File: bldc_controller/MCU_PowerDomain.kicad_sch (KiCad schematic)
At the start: 10 parts, among them U2 STM32G474CEUx

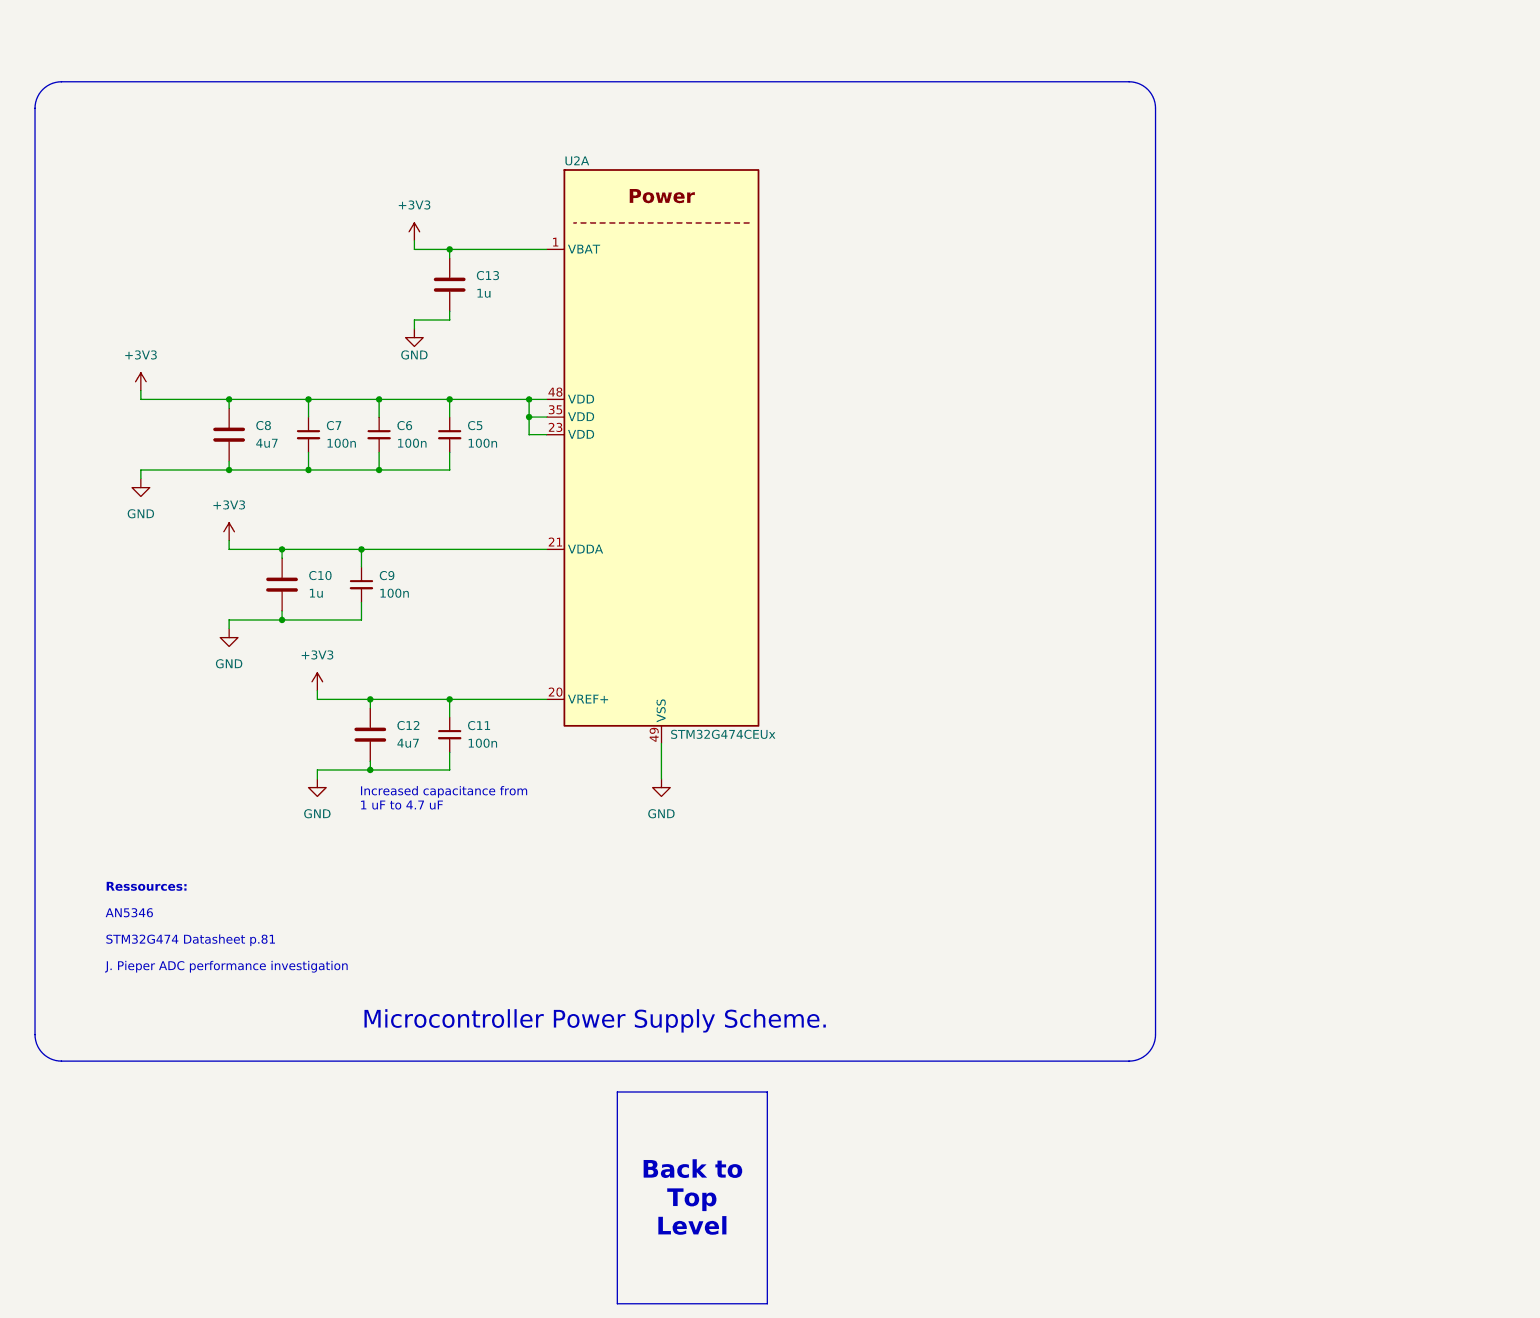
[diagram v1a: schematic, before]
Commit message: added temporary footprints and deleted extra files
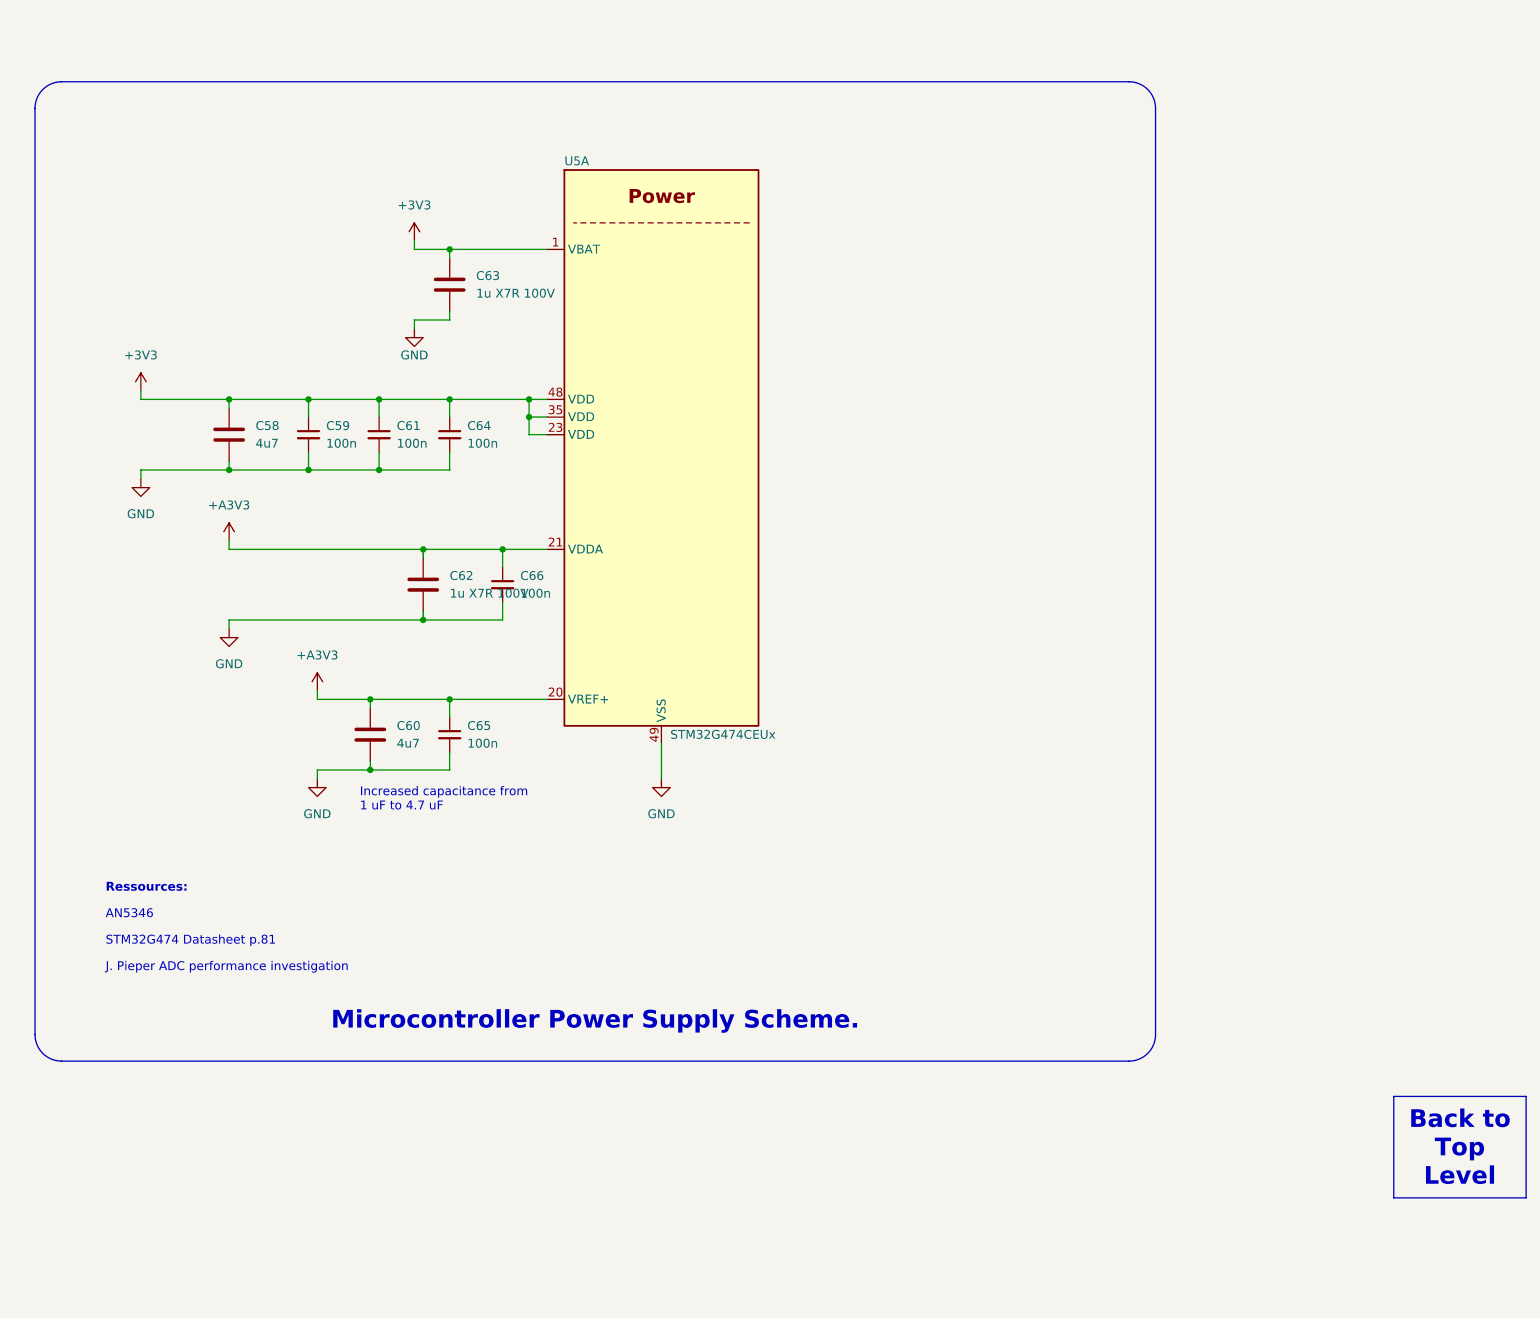
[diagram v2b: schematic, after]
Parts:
- C58: renamed from C8; footprint (none) -> Capacitor_SMD:C_0603_1608Metric
- C59: renamed from C7; footprint (none) -> Capacitor_SMD:C_0402_1005Metric
- C60: renamed from C12; footprint (none) -> Capacitor_SMD:C_0603_1608Metric
- C61: renamed from C6; footprint (none) -> Capacitor_SMD:C_0402_1005Metric
- C62: renamed from C10; value 1u -> 1u X7R 100V; footprint (none) -> Capacitor_SMD:C_0402_1005Metric
- C63: renamed from C13; value 1u -> 1u X7R 100V; footprint (none) -> Capacitor_SMD:C_0402_1005Metric
- C64: renamed from C5; footprint (none) -> Capacitor_SMD:C_0402_1005Metric
- C65: renamed from C11; footprint (none) -> Capacitor_SMD:C_0402_1005Metric
- C66: renamed from C9; footprint (none) -> Capacitor_SMD:C_0402_1005Metric
- renumbered U2 to U5
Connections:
- net +3V3: no longer C60.1, C62.1, C65.1, C66.1, U5.20 (VREF+), U5.21 (VDDA)
- new net +A3V3: C60.1, C62.1, C65.1, C66.1, U5.20 (VREF+), U5.21 (VDDA)
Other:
- moved on the sheet: C62, C66

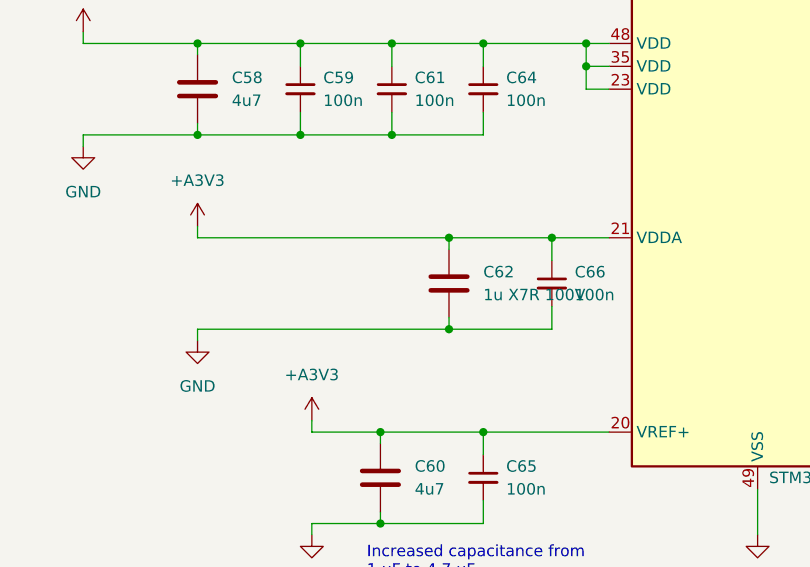
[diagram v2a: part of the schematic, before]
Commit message: added IPC-7351 compliant footprints and started routing
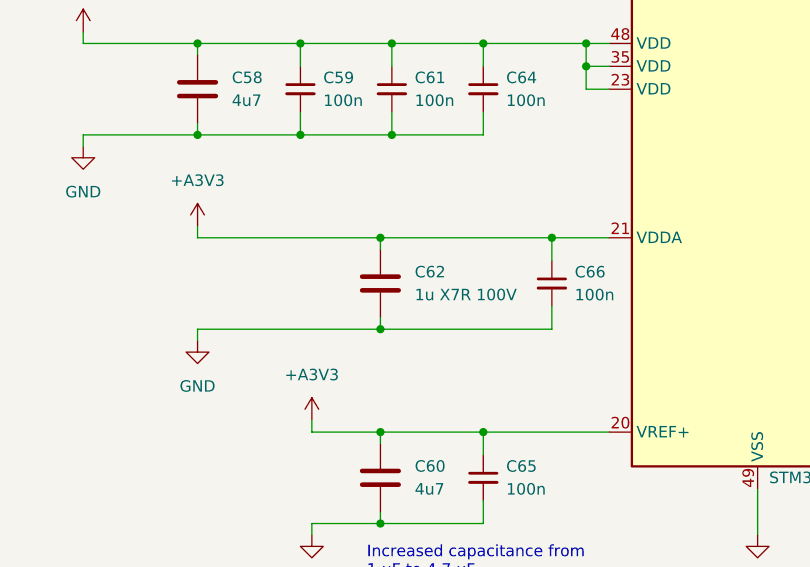
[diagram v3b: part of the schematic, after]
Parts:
- C58, C60: footprint Capacitor_SMD:C_0603_1608Metric -> 0_capacitor_smd:C_0603_1608_DensityHigh
- C59, C61, C62, C63, C64, C65, C66: footprint Capacitor_SMD:C_0402_1005Metric -> 0_capacitor_smd:C_0402_1005_DensityHigh
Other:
- moved on the sheet: C62
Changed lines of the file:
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@@
   (junction (at 109.22 66.04) (diameter 0) (color 0 0 0 0)
   )
-  (junction (at 125.73 87.63) (diameter 0) (color 0 0 0 0)
-  )
   (junction (at 129.54 44.45) (diameter 0) (color 0 0 0 0)
   )
+  (junction (at 118.11 97.79) (diameter 0) (color 0 0 0 0)
+  )
   (junction (at 140.97 66.04) (diameter 0) (color 0 0 0 0)
   )
@@
   (junction (at 109.22 76.2) (diameter 0) (color 0 0 0 0)
   )
-  (junction (at 125.73 97.79) (diameter 0) (color 0 0 0 0)
-  )
   (junction (at 97.79 76.2) (diameter 0) (color 0 0 0 0)
   )
@@
   (junction (at 118.11 119.38) (diameter 0) (color 0 0 0 0)
   )
+  (junction (at 118.11 87.63) (diameter 0) (color 0 0 0 0)
+  )
   (wire (pts (xy 119.38 76.2) (xy 129.54 76.2))
     (stroke (width 0) (type default))
@@
     (stroke (width 0) (type default))
   )
-  (wire (pts (xy 125.73 87.63) (xy 125.73 88.9))
-    (stroke (width 0) (type default))
-  )
-  (wire (pts (xy 125.73 97.79) (xy 137.16 97.79))
+  (wire (pts (xy 118.11 87.63) (xy 118.11 88.9))
     (stroke (width 0) (type default))
   )
@@
     (stroke (width 0) (type default))
   )
-  (wire (pts (xy 125.73 96.52) (xy 125.73 97.79))
+  (wire (pts (xy 118.11 96.52) (xy 118.11 97.79))
     (stroke (width 0) (type default))
   )
@@
     (stroke (width 0) (type default))
   )
+  (wire (pts (xy 118.11 97.79) (xy 137.16 97.79))
+    (stroke (width 0) (type default))
+  )
   (wire (pts (xy 129.54 111.76) (xy 129.54 109.22))
     (stroke (width 0) (type default))
@@
     (stroke (width 0) (type default))
   )
-  (wire (pts (xy 97.79 87.63) (xy 125.73 87.63))
+  (wire (pts (xy 97.79 87.63) (xy 118.11 87.63))
     (stroke (width 0) (type default))
   )
@@
     (stroke (width 0) (type default))
   )
-  (wire (pts (xy 137.16 87.63) (xy 125.73 87.63))
-    (stroke (width 0) (type default))
-  )
-  (wire (pts (xy 97.79 97.79) (xy 125.73 97.79))
+  (wire (pts (xy 97.79 97.79) (xy 118.11 97.79))
     (stroke (width 0) (type default))
   )
@@
   )
   (wire (pts (xy 109.22 76.2) (xy 119.38 76.2))
+    (stroke (width 0) (type default))
+  )
+  (wire (pts (xy 118.11 87.63) (xy 137.16 87.63))
     (stroke (width 0) (type default))
   )
@@
       (effects (font (size 1.27 1.27)) (justify left))
     )
-    (property "Footprint" "Capacitor_SMD:C_0402_1005Metric" (at 109.22 71.12 0)
+    (property "Footprint" "0_capacitor_smd:C_0402_1005_DensityHigh" (at 109.22 71.12 0)
       (effects (font (size 1.27 1.27)) hide)
     )
@@
       (effects (font (size 1.27 1.27)) (justify left))
     )
-    (property "Footprint" "Capacitor_SMD:C_0402_1005Metric" (at 137.16 92.71 0)
+    (property "Footprint" "0_capacitor_smd:C_0402_1005_DensityHigh" (at 137.16 92.71 0)
       (effects (font (size 1.27 1.27)) hide)
     )
@@
       (effects (font (size 1.27 1.27)) (justify left))
     )
-    (property "Footprint" "Capacitor_SMD:C_0402_1005Metric" (at 129.54 71.12 0)
+    (property "Footprint" "0_capacitor_smd:C_0402_1005_DensityHigh" (at 129.54 71.12 0)
       (effects (font (size 1.27 1.27)) hide)
     )
@@
       (effects (font (size 1.27 1.27)) (justify left))
     )
-    (property "Footprint" "Capacitor_SMD:C_0603_1608Metric" (at 119.0752 118.11 0)
+    (property "Footprint" "0_capacitor_smd:C_0603_1608_DensityHigh" (at 119.0752 118.11 0)
       (effects (font (size 1.27 1.27)) hide)
     )
@@
     )
   )
-  (symbol (lib_id "Device:C") (at 125.73 92.71 0) (unit 1)
-    (in_bom yes) (on_board yes) (dnp no)
-    (property "Reference" "C62" (at 129.54 91.44 0)
-      (effects (font (size 1.27 1.27)) (justify left))
-    )
-    (property "Value" "1u X7R 100V" (at 129.54 93.98 0)
-      (effects (font (size 1.27 1.27)) (justify left))
-    )
-    (property "Footprint" "Capacitor_SMD:C_0402_1005Metric" (at 126.6952 96.52 0)
-      (effects (font (size 1.27 1.27)) hide)
-    )
-    (property "Datasheet" "~" (at 125.73 92.71 0)
+  (symbol (lib_id "Device:C") (at 118.11 92.71 0) (unit 1)
+    (in_bom yes) (on_board yes) (dnp no)
+    (property "Reference" "C62" (at 121.92 91.44 0)
+      (effects (font (size 1.27 1.27)) (justify left))
+    )
+    (property "Value" "1u X7R 100V" (at 121.92 93.98 0)
+      (effects (font (size 1.27 1.27)) (justify left))
+    )
+    (property "Footprint" "0_capacitor_smd:C_0402_1005_DensityHigh" (at 119.0752 96.52 0)
+      (effects (font (size 1.27 1.27)) hide)
+    )
+    (property "Datasheet" "~" (at 118.11 92.71 0)
       (effects (font (size 1.27 1.27)) hide)
     )
@@
       (effects (font (size 1.27 1.27)) (justify left))
     )
-    (property "Footprint" "Capacitor_SMD:C_0402_1005Metric" (at 130.5052 53.34 0)
+    (property "Footprint" "0_capacitor_smd:C_0402_1005_DensityHigh" (at 130.5052 53.34 0)
       (effects (font (size 1.27 1.27)) hide)
     )
@@
       (effects (font (size 1.27 1.27)) (justify left))
     )
-    (property "Footprint" "Capacitor_SMD:C_0402_1005Metric" (at 129.54 114.3 0)
+    (property "Footprint" "0_capacitor_smd:C_0402_1005_DensityHigh" (at 129.54 114.3 0)
       (effects (font (size 1.27 1.27)) hide)
     )
@@
       (effects (font (size 1.27 1.27)) (justify left))
     )
-    (property "Footprint" "Capacitor_SMD:C_0402_1005Metric" (at 119.38 71.12 0)
+    (property "Footprint" "0_capacitor_smd:C_0402_1005_DensityHigh" (at 119.38 71.12 0)
       (effects (font (size 1.27 1.27)) hide)
     )
@@
       (effects (font (size 1.27 1.27)) (justify left))
     )
-    (property "Footprint" "Capacitor_SMD:C_0603_1608Metric" (at 98.7552 74.93 0)
-      (effects (font (size 1.27 1.27)) hide)
-    )
+    (property "Footprint" "0_capacitor_smd:C_0603_1608_DensityHigh" (at 98.7552 74.93 0)
+      (effects (font (size 1.27 1.27)) hide)
+    )

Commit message: some progress on the pcb
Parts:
- C60: footprint 0_capacitor_smd:C_0603_1608_DensityHigh -> 0_capacitor_smd:C_0402_1005_DensityHigh
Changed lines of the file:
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@@
       (effects (font (size 1.27 1.27)) (justify left))
     )
-    (property "Footprint" "0_capacitor_smd:C_0603_1608_DensityHigh" (at 119.0752 118.11 0)
+    (property "Footprint" "0_capacitor_smd:C_0402_1005_DensityHigh" (at 119.0752 118.11 0)
       (effects (font (size 1.27 1.27)) hide)
     )
